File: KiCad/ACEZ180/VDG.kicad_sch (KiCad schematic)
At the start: 32 parts

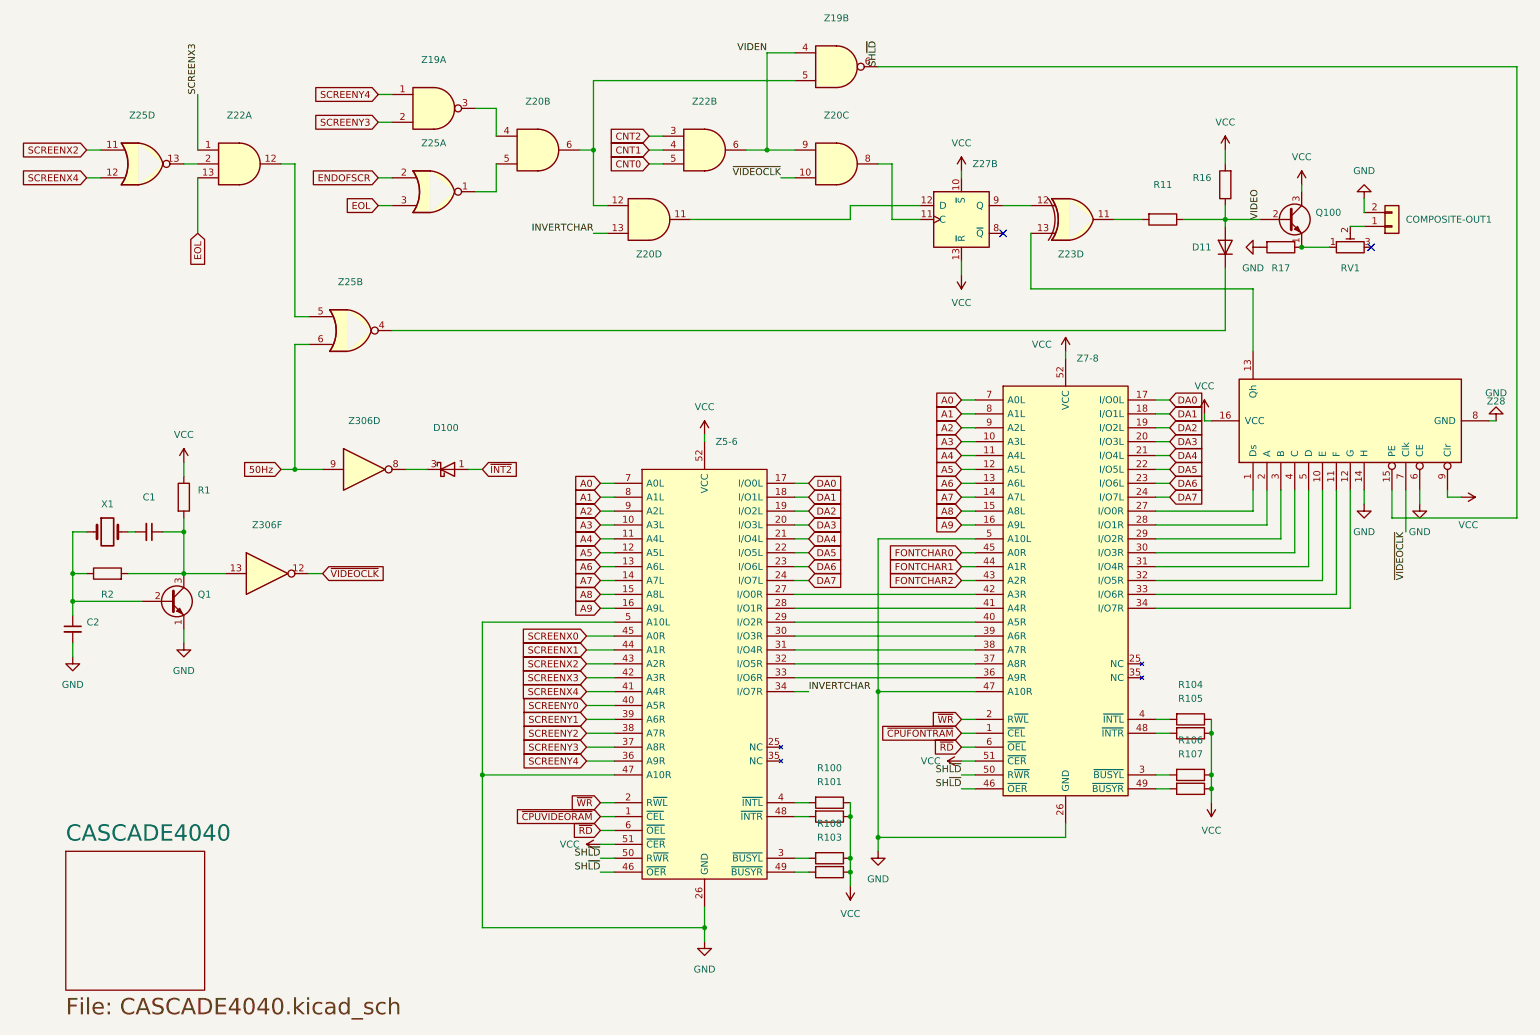
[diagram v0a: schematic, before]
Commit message: Fix mistake with ROM Select.
Signed-off-by: John Bradley <flypie@rocketmail.com>
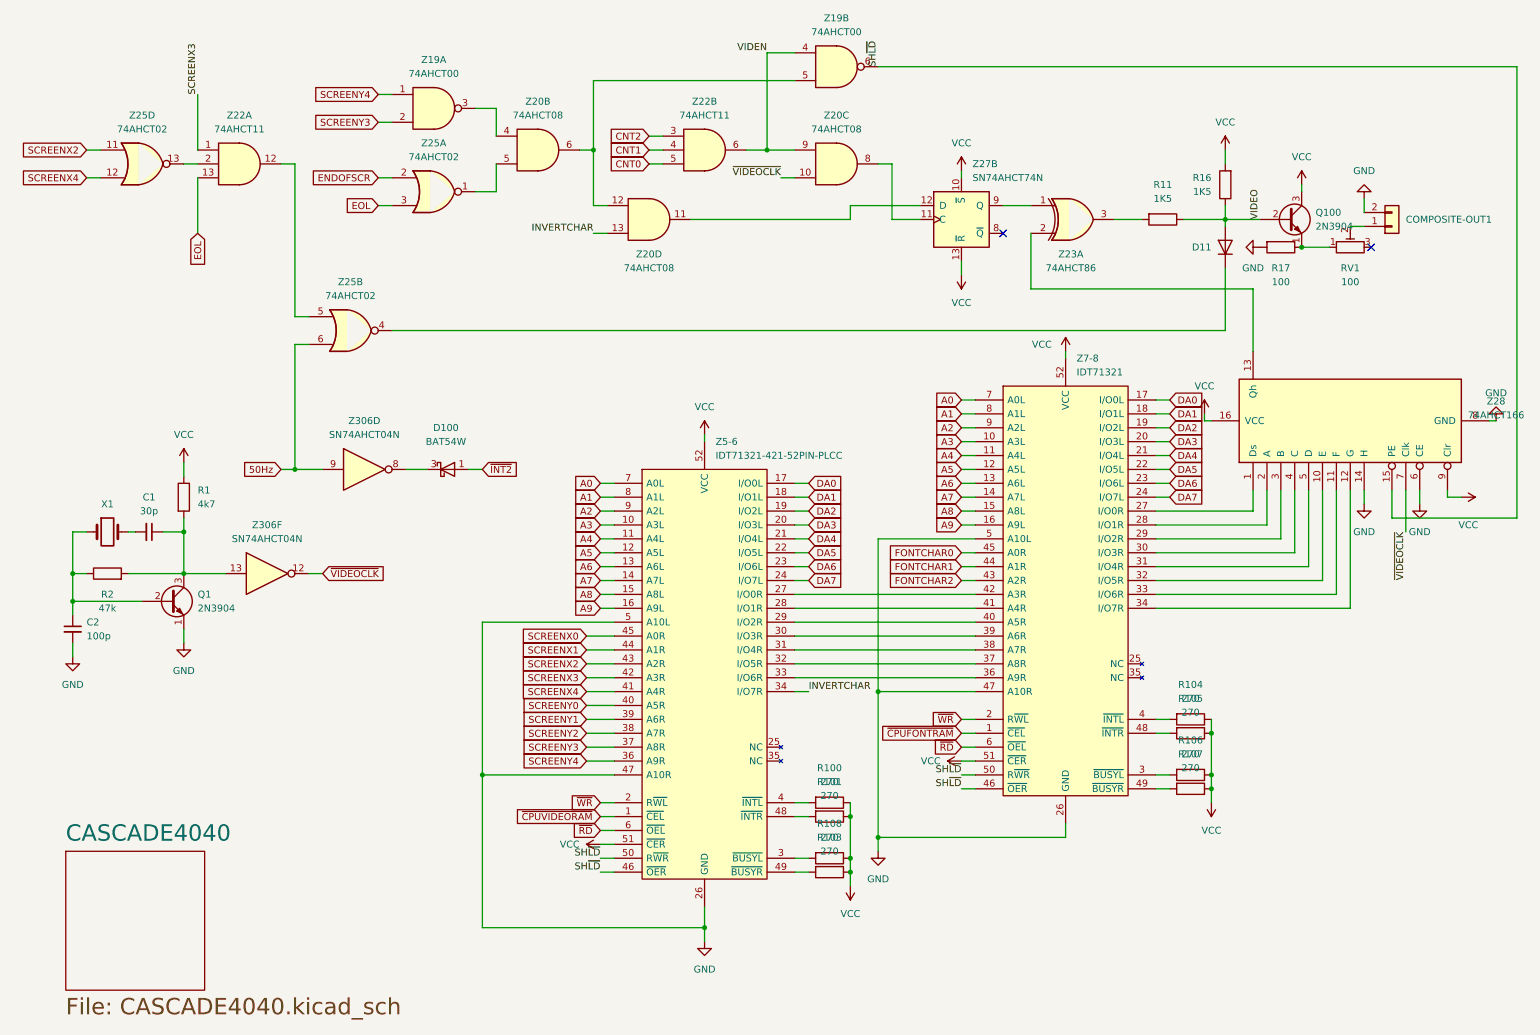
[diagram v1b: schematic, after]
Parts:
- C1: value (none) -> 30p; footprint (none) -> Capacitor_THT:C_Disc_D3.0mm_W1.6mm_P2.50mm
- C2: value (none) -> 100p; footprint (none) -> Capacitor_THT:C_Disc_D3.0mm_W1.6mm_P2.50mm
- COMPOSITE-OUT1: value (none) -> COMPOSITE-OUT1; footprint (none) -> Connector_PinHeader_2.54mm:PinHeader_1x02_P2.54mm_Vertical
- D100: value (none) -> BAT54W; footprint (none) -> Package_TO_SOT_SMD:SOT-323_SC-70
- D11: value (none) -> 1N4148; footprint (none) -> Diode_THT:D_DO-35_SOD27_P2.54mm_Vertical_AnodeUp
- Q1, Q100: value (none) -> 2N3904; footprint (none) -> Package_TO_SOT_THT:TO-92_Inline
- R1: value (none) -> 4k7; footprint (none) -> Resistor_THT:R_Axial_DIN0204_L3.6mm_D1.6mm_P1.90mm_Vertical
- R100, R101, R103, R104, R105, R106, R107, R108: value (none) -> 270; footprint (none) -> Resistor_THT:R_Axial_DIN0204_L3.6mm_D1.6mm_P2.54mm_Vertical
- R11, R16: value (none) -> 1K5; footprint (none) -> Resistor_THT:R_Axial_DIN0204_L3.6mm_D1.6mm_P2.54mm_Vertical
- R17: value (none) -> 100; footprint (none) -> Resistor_THT:R_Axial_DIN0204_L3.6mm_D1.6mm_P2.54mm_Vertical
- R2: value (none) -> 47k; footprint (none) -> Resistor_THT:R_Axial_DIN0204_L3.6mm_D1.6mm_P2.54mm_Vertical
- RV1: value (none) -> 100; footprint (none) -> ExtraFootprints:3362H1103LF
- X1: value (none) -> CRYSTALHC49U-V 6.556MHz; footprint (none) -> Crystal:Crystal_HC49-U_Vertical
- Z19: value (none) -> 74AHCT00; footprint (none) -> Package_DIP:DIP-14_W7.62mm_Socket
- Z20: value (none) -> 74AHCT08; footprint (none) -> Package_DIP:DIP-14_W7.62mm_Socket
- Z22: value (none) -> 74AHCT11; footprint (none) -> Package_DIP:DIP-14_W7.62mm_Socket
- Z23: value (none) -> 74AHCT86; footprint (none) -> Package_DIP:DIP-14_W7.62mm_Socket
- Z25: value (none) -> 74AHCT02; footprint (none) -> Package_DIP:DIP-14_W7.62mm_Socket
- Z27: value (none) -> SN74AHCT74N; footprint (none) -> Package_DIP:DIP-14_W7.62mm_Socket
- Z28: value (none) -> 74AHCT166; footprint (none) -> Package_DIP:DIP-16_W7.62mm_Socket
- Z306: value (none) -> SN74AHCT04N; footprint (none) -> Package_DIP:DIP-14_W7.62mm_Socket
- Z5-6: value (none) -> IDT71321-421-52PIN-PLCC; footprint (none) -> Package_LCC:PLCC-52
- Z7-8: value (none) -> IDT71321; footprint (none) -> Package_LCC:PLCC-52
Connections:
- net at R11.2: now also Z23.3; no longer Z23.11
- net at Z27.9 (Q): now also Z23.1; no longer Z23.12
- net at Z28.13 (Qh): now also Z23.2; no longer Z23.13
